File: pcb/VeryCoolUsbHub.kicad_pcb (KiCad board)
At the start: 2 copper layers, 49 parts, among them U1 HD3SS3220RNHR, U2 HD3SS3220RNHR, X1 X322525MSB4SI, X2 X322525MSB4SI

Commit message: BIG UPDATEEEEEEEEE
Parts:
- added C25: CC0603JRNPO9BN390, EasyEDA:C0603, F.Cu at (207.7, 54.3)
- added R2: RC0402FR-0710KL, EasyEDA:R0402, F.Cu at (214.1, 39.1)
- C1, C2, C28, C29, C3, C30, C31, C32, C4, R6: moved to B.Cu
- moved RJ45 155.5 mm to (233.3, 27.6)
- moved USBC_OUT_1 144.3 mm to (243.3, 53.3), turned to 90 degrees
- moved C7 141.6 mm to (244.3, 42.5), turned to -90 degrees
- moved C3 139.3 mm to (246.2, 51.2)
- moved C4 139.0 mm to (246.2, 56.0)
- moved C2 138.7 mm to (246.2, 52.8)
- moved X1 138.3 mm to (240.7, 42.5)
- moved C1 138.3 mm to (246.2, 54.4)
- moved C6 136.5 mm to (240.5, 45.4), turned to 180 degrees
- moved R9 132.3 mm to (225.4, 51.3)
- moved C12 131.7 mm to (239.7, 37.7), turned to 180 degrees
- moved R6 130.6 mm to (233.3, 22.4), turned to 180 degrees
- moved C16 127.4 mm to (235.3, 48.8), turned to 180 degrees
- moved C15 127.1 mm to (235.3, 47.1), turned to 180 degrees
- moved USB_OUT2 125.5 mm to (227.5, 68.8), turned to 180 degrees
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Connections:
- USBC_IN_1 pad 0: unconnected-(USBC_IN_1-EH-Pad0) -> GND
- USB_CONTROLLER1 pad 24: unconnected-(USB_CONTROLLER1-RESETJ-Pad24) -> Net-(USB_CONTROLLER1-RESETJ)
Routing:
- net VBUS: track 13.4 -> 306.7 mm, vias 3 -> 12
- net /V3.3: track 2.57 -> 78.8 mm, vias 2 -> 8
- net /DN0: track 9.16 -> 52.4 mm, vias 2 -> 3
- net /DP0: track 8.09 -> 46.8 mm, vias 2 -> 3
- net /DN3: track 0.00 -> 31.5 mm, vias 0 -> 3
- net /DP3: track 0.00 -> 30.5 mm, vias 0 -> 3
- net /Txp2: track 0.00 -> 29.3 mm, vias 0 -> 1
- net /Txn2: track 0.00 -> 28.7 mm, vias 0 -> 1
- net /LED1: track 0.00 -> 27.1 mm, vias 0 -> 1
- net /LED2: track 0.00 -> 26.9 mm, vias 0 -> 1
- net /RXp2: track 0.00 -> 26.1 mm
- net /DN2: track 0.00 -> 25.9 mm
- net /Txn1: track 0.00 -> 25.6 mm, vias 0 -> 1
- net /RXn2: track 0.00 -> 25.4 mm
- net /Txp1: track 0.00 -> 24.8 mm, vias 0 -> 1
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- added copper zone on B.Cu, net GND
- added copper zone on F.Cu, net GND
- added copper zone on In1.Cu, net GND
- added copper zone on In2.Cu, net GND
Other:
- board outline added: 73.7 x 58.2 mm
- copper layers 2 -> 4
- board text added: "usb controller"

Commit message: please tell me this is the last time i need to reroute
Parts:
- added C26: CC0603KRX7R9BB104, EasyEDA:C0603, F.Cu at (114.6, 62.9)
- added C27: CC0603KRX7R9BB104, EasyEDA:C0603, F.Cu at (114.6, 65.6)
- added C33: CC0603KRX7R9BB104, EasyEDA:C0603, F.Cu at (118.7, 57.6)
- added C34: CC0603KRX7R9BB104, EasyEDA:C0603, F.Cu at (118.7, 60.3)
- C1, C2, C28, C29, C3, C30, C31, C32, C4, R6: moved to F.Cu
- moved C1 140.0 mm to (106.6, 44.2)
- moved C2 139.7 mm to (106.6, 46.9)
- moved C4 139.7 mm to (106.6, 52.2)
- moved C3 139.6 mm to (106.6, 49.6)
- moved C7 138.9 mm to (106.6, 60.3), turned to 0 degrees
- moved C6 134.5 mm to (106.6, 57.6), turned to 0 degrees
- moved C12 129.6 mm to (110.6, 49.6), turned to 0 degrees
- moved C11 126.2 mm to (110.6, 46.9), turned to 0 degrees
- moved C16 125.2 mm to (110.6, 60.3), turned to 0 degrees
- moved C15 125.1 mm to (110.6, 57.6), turned to 0 degrees
- moved C24 122.1 mm to (114.6, 57.6), turned to 0 degrees
- moved C23 122.0 mm to (114.6, 54.9), turned to 0 degrees
- moved C14 121.7 mm to (110.6, 54.9), turned to 0 degrees
- moved C13 118.6 mm to (110.6, 52.2), turned to 0 degrees
- moved C19 117.5 mm to (114.6, 44.2), turned to 0 degrees
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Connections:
- net /RXn0 renamed /RXN0
- net /RXn1 renamed /RXN1
- net /RXn2 renamed /RXN2
- net /RXn3 renamed /RXN3
- net /RXn4 renamed /RXN4
- net /RXp0 renamed /RXP0
- net /RXp1 renamed /RXP1
- net /RXp2 renamed /RXP2
- net /RXp3 renamed /RXP3
- net /RXp4 renamed /RXP4
- net /Txn0 renamed /TXN0
- net /Txn3 renamed /TXN3
- net /Txn4 renamed /TXN4
- net /Txp0 renamed /TXP0
- net /Txp3 renamed /TXP3
- net /Txp4 renamed /TXP4
- USB_CONTROLLER1 pad 47: /Txn1 -> /TXN1
- USB_CONTROLLER1 pad 48: /Txp1 -> /TXP1
- USB_CONTROLLER1 pad 56: /Txn2 -> /TXN2
- USB_CONTROLLER1 pad 57: /Txp2 -> /TXP2
- USB_OUT1 pad 8: /Txn1 -> Net-(USB_OUT1-SSTX-)
- USB_OUT1 pad 9: /Txp1 -> Net-(USB_OUT1-SSTX+)
- USB_OUT2 pad 8: /Txn2 -> Net-(USB_OUT2-SSTX-)
- USB_OUT2 pad 9: /Txp2 -> Net-(USB_OUT2-SSTX+)
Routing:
- net VBUS: track 306.7 -> 8.15 mm, vias 12 -> 4
- net /V3.3: track 78.8 -> 3.42 mm, vias 8 -> 2
- net /DN3: track 31.5 -> 0.00 mm, vias 3 -> 0
- net /DP3: track 30.5 -> 0.00 mm, vias 3 -> 0
- net /Txp2: track 29.3 -> 0.00 mm, vias 1 -> 0
- net /Txn2: track 28.7 -> 0.00 mm, vias 1 -> 0
- net /LED1: track 27.1 -> 0.00 mm, vias 1 -> 0
- net /LED2: track 26.9 -> 0.00 mm, vias 1 -> 0
- net /RXP2: track 26.1 -> 0.00 mm
- net /DN2: track 25.9 -> 0.00 mm
- net /Txn1: track 25.6 -> 0.00 mm, vias 1 -> 0
- net /RXN2: track 25.4 -> 0.00 mm
- net /Txp1: track 24.8 -> 0.00 mm, vias 1 -> 0
- net /RXN1: track 24.6 -> 0.00 mm
- net /DP2: track 24.5 -> 0.00 mm
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- removed copper zone on B.Cu, net GND
- removed copper zone on F.Cu, net GND
- removed copper zone on In1.Cu, net GND
- removed copper zone on In2.Cu, net GND
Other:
- board outline removed
- board text removed: "usb controller"

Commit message: oops forgot to save
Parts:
- removed C10, C26, C27: CC0603KRX7R9BB104, EasyEDA:C0603
- removed USB_OUT1, USB_OUT2: HC-USB3.0-L168-WP, EasyEDA:USB-TH_USB3.0-A
- added C35: CC0603KRX7R9BB104, EasyEDA:C0603, F.Cu at (233.2, 64.7)
- added C36: CC0603KRX7R9BB104, EasyEDA:C0603, B.Cu at (224.2, 65.0)
- added C37: CC0603KRX7R9BB104, EasyEDA:C0603, B.Cu at (225.8, 65.0)
- added R4: R, Resistor_SMD:R_0402_1005Metric, F.Cu at (227.7, 33.2)
- added USB_OUT_1: HC-ST-003-01-J, EasyEDA:USB-3.0-A-TH_HC-ST-003-01-Z, F.Cu at (206.3, 69.6)
- added USB_OUT_2: HC-ST-003-01-J, EasyEDA:USB-3.0-A-TH_HC-ST-003-01-Z, F.Cu at (235.1, 69.7)
- C1, C11, C12, C13, C14, C15, C16, C2, C28, C29, C3, C30, C33, C4: moved to B.Cu
- moved C1 153.1 mm to (259.5, 52.4)
- moved C4 153.0 mm to (259.5, 47.8)
- moved C2 153.0 mm to (259.5, 50.9)
- moved C3 152.9 mm to (259.5, 49.4)
- moved C16 131.0 mm to (239.1, 34.6)
- moved C6 130.4 mm to (234.7, 33.5), turned to 180 degrees
- moved C24 129.9 mm to (244.3, 49.8), turned to 180 degrees
- moved C23 129.8 mm to (244.3, 48.3), turned to 180 degrees
- moved C13 129.5 mm to (239.1, 36.2)
- moved C15 129.5 mm to (239.0, 40.9), turned to 180 degrees
- moved C14 129.3 mm to (239.0, 39.3), turned to 180 degrees
- moved C7 128.3 mm to (231.1, 29.3)
- moved C19 127.0 mm to (241.6, 46.5), turned to 180 degrees
- moved C17 113.7 mm to (222.5, 42.5)
- moved C5 111.7 mm to (217.6, 42.5), turned to 180 degrees
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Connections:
- C11 pad 1: VBUS -> Net-(USB_OUT_1-StdA_SSTX-)
- C11 pad 2: GND -> /TXN1
- C33 pad 2: /TXN2 -> /TXP1
- C34 pad 1: Net-(USB_OUT2-SSTX+) -> VBUS
- C34 pad 2: /TXP2 -> GND
- ETHERNET_CONTROLLER1 pad 38: unconnected-(ETHERNET_CONTROLLER1-RSET-Pad38) -> Net-(ETHERNET_CONTROLLER1-RSET)
- USBC_OUT_1 pad 0: unconnected-(USBC_OUT_1-EH-Pad0) -> GND
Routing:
- net /V3.3: track 3.42 -> 220.7 mm, vias 2 -> 8
- net VBUS: track 8.15 -> 217.5 mm, vias 4 -> 13
- net GND: track 6.98 -> 75.5 mm, vias 8 -> 46
- net /RXN2: track 0.00 -> 43.0 mm
- net /RXP2: track 0.00 -> 40.9 mm
- net /USBC_OUT_RXN1: track 0.00 -> 40.4 mm
- net /USBC_OUT_CC1: track 0.00 -> 40.2 mm, vias 0 -> 2
- net /DN1: track 0.00 -> 39.9 mm
- net /DP1: track 0.00 -> 38.7 mm
- net /USBC_OUT_RXP1: track 0.00 -> 38.5 mm
- net /DP2: track 0.00 -> 38.3 mm
- net /LED2: track 0.00 -> 38.1 mm
- net /DP3: track 0.00 -> 37.4 mm, vias 0 -> 3
- net /DN2: track 0.00 -> 37.1 mm
- net /RXP1: track 0.00 -> 36.6 mm
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- added copper zone on B.Cu, net GND
- added copper zone on In1.Cu, net GND
- added copper zone on In2.Cu, net GND
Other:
- board outline added: 84.8 x 58.4 mm

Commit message: LETSGO THIS GONNA BE THE LAST TIME I ROUTE
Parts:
- added C10: CC0603KRX7R9BB104, EasyEDA:C0603, F.Cu at (230.7, 60.8)
- added C26: CC0603KRX7R9BB104, EasyEDA:C0603, F.Cu at (230.7, 62.3)
- C11, C12, C13, C14, C15, C16, C33, C36, C37: moved to F.Cu
- C31, C32, R6: moved to B.Cu
- moved C16 25.5 mm to (220.5, 52.1)
- moved C13 23.5 mm to (220.5, 50.5)
- moved C31 22.7 mm to (167.4, 57.3), turned to 0 degrees
- moved C32 22.7 mm to (167.4, 55.8), turned to 180 degrees
- moved R4 22.3 mm to (209.2, 45.6), turned to 180 degrees
- moved RJ45 21.3 mm to (200.1, 38.4)
- moved ETHERNET_CONTROLLER1 21.2 mm to (212.7, 48.9)
- moved C6 20.8 mm to (216.2, 43.1), turned to -90 degrees
- moved C14 20.7 mm to (219.6, 46.4)
- moved C15 20.7 mm to (219.6, 48.0)
- moved X1 20.7 mm to (213.3, 43.0)
- moved C7 20.7 mm to (213.2, 39.6)
- moved C35 20.2 mm to (216.2, 75.7), turned to 90 degrees
- moved C4 19.6 mm to (242.2, 57.1)
- moved C19 19.5 mm to (223.1, 52.7), turned to -90 degrees
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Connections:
- C11 pad 2: /TXN1 -> /TXP1
- C20 pad 1: /USBC_IN_TXP2 -> /USBC_IN_TXN2
- C21 pad 1: /USBC_IN_TXN2 -> /USBC_IN_TXP2
- C23 pad 1: /USBC_OUT_TXP2 -> /USBC_OUT_TXN2
- C24 pad 1: /USBC_OUT_TXN2 -> /USBC_OUT_TXP2
- C33 pad 2: /TXP1 -> /TXN1
- C35 pad 1: Net-(USB_OUT_2-Vbus) -> VBUS
- C36 pad 2: /TXN2 -> /TXP2
- C37 pad 2: /TXP2 -> /TXN2
- C8 pad 1: /USBC_IN_TXN1 -> /USBC_IN_TXP1
- C9 pad 2: /USBC_IN_TXP1 -> /USBC_IN_TXN1
- ETHERNET_CONTROLLER1 pad 12: /TXN4 -> /TXP4
- ETHERNET_CONTROLLER1 pad 13: /TXP4 -> /TXN4
- ETHERNET_CONTROLLER1 pad 15: /RXN4 -> /RXP4
- ETHERNET_CONTROLLER1 pad 16: /RXP4 -> /RXN4
- U1 pad 16: /USBC_OUT_TXN1 -> Net-(U1-TX1n)
- U1 pad 17: /USBC_OUT_TXP1 -> Net-(U1-TX1p)
- USB_OUT_1 pad 5: /RXN1 -> /RXP1
- USB_OUT_1 pad 6: /RXP1 -> /RXN1
- USB_OUT_2 pad 1: Net-(USB_OUT_2-Vbus) -> VBUS
- USB_OUT_2 pad 5: /RXN2 -> /RXP2
- USB_OUT_2 pad 6: /RXP2 -> /RXN2
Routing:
- net /V3.3: track 220.7 -> 104.0 mm, vias 8 -> 7
- net VBUS: track 217.5 -> 285.5 mm, vias 13 -> 12
- net GND: track 75.5 -> 101.7 mm, vias 46 -> 37
- net /RXP1: track 36.6 -> 16.9 mm
- net /RXN1: track 35.6 -> 16.9 mm
- net /USBC_IN_CC2: track 25.5 -> 42.0 mm
- net /DN2: track 37.1 -> 53.3 mm
- net /USBC_OUT_TXN2: track 12.3 -> 27.6 mm, vias 2 -> 0
- net /USBC_OUT_TXP2: track 12.5 -> 26.3 mm, vias 2 -> 0
- net /DP2: track 38.3 -> 52.1 mm
- net /USBC_IN_RXP1: track 22.2 -> 35.8 mm
- net /RXN2: track 43.0 -> 29.3 mm
- net /USBC_IN_TXN2: track 16.1 -> 29.7 mm, vias 2 -> 0
- net /USBC_IN_RXN1: track 24.1 -> 37.7 mm
- net Net-(USB_OUT_2-StdA_SSTX-): track 21.9 -> 8.87 mm
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- removed copper zone on B.Cu, net GND
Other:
- board size 84.8 x 58.4 mm -> 80.7 x 55.9 mm

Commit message: maybedone?
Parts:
- added G***: LOGO, LOGO, F.Cu at (229.0, 49.2)
- added G***: LOGO, LOGO, F.Cu at (240.0, 74.4)
- added G***: LOGO, LOGO, F.Cu at (179.6, 35.8)
- added G***: LOGO, LOGO, F.Cu at (172.7, 31.7)
- added G***: LOGO, LOGO, F.Cu at (233.1, 35.2)
- added G***: LOGO, LOGO, F.Cu at (187.6, 72.7)
- added G***: LOGO, LOGO, F.Cu at (174.4, 46.0)
- moved R2 1.36 mm to (204.5, 52.4)
- moved C5 1.34 mm to (201.2, 52.4)
- moved C17 1.14 mm to (207.5, 52.1)
- renumbered USBC_IN_1 to USB_IN_1
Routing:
- net VBUS: track 285.5 -> 331.4 mm, vias 12 -> 11
- net GND: track 101.7 -> 116.4 mm, vias 37 -> 40
- net /USBC_IN_RXP1: track 35.8 -> 28.0 mm
- net /USBC_IN_RXN1: track 37.7 -> 29.9 mm
- net /USBC_IN_TXN2: track 29.7 -> 22.2 mm
- net /USBC_IN_TXP2: track 28.5 -> 20.9 mm
- net /USBC_IN_CC2: track 42.0 -> 40.4 mm
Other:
- outline, holes or cut-outs redrawn
- board text added: "1 Gb Ethernetport"
- board text added: "@duykhanh09103"
- board text added: "Ethernet Controler"
- board text added: "Opensource project!!"
- board text added: "Specical shoutout: TobyCM Arca Keyaan Astra Celestine Cyao"
- board text added: "USB A DOWNSTREAM"
- board text added: "USB C DOWNSTREAM"
- board text added: "USB C UPSTREAM"
- board text added: "USB Controller"
- board text added: "made with love from duykhanh09103 <3 me@duykhanh09103.dev"

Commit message: i think im done with pcb
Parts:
- added G***: LOGO, LOGO, B.Cu at (212.1, 57.0)
- added G***: LOGO, LOGO, B.Cu at (171.0, 37.7)
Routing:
- net GND: track 116.4 -> 114.8 mm, vias 40 -> 39
- net VBUS: track 331.4 -> 330.3 mm
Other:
- board text added: "This project is sponsored by fallout!!"
- board text added: "pss, join hackclub here"

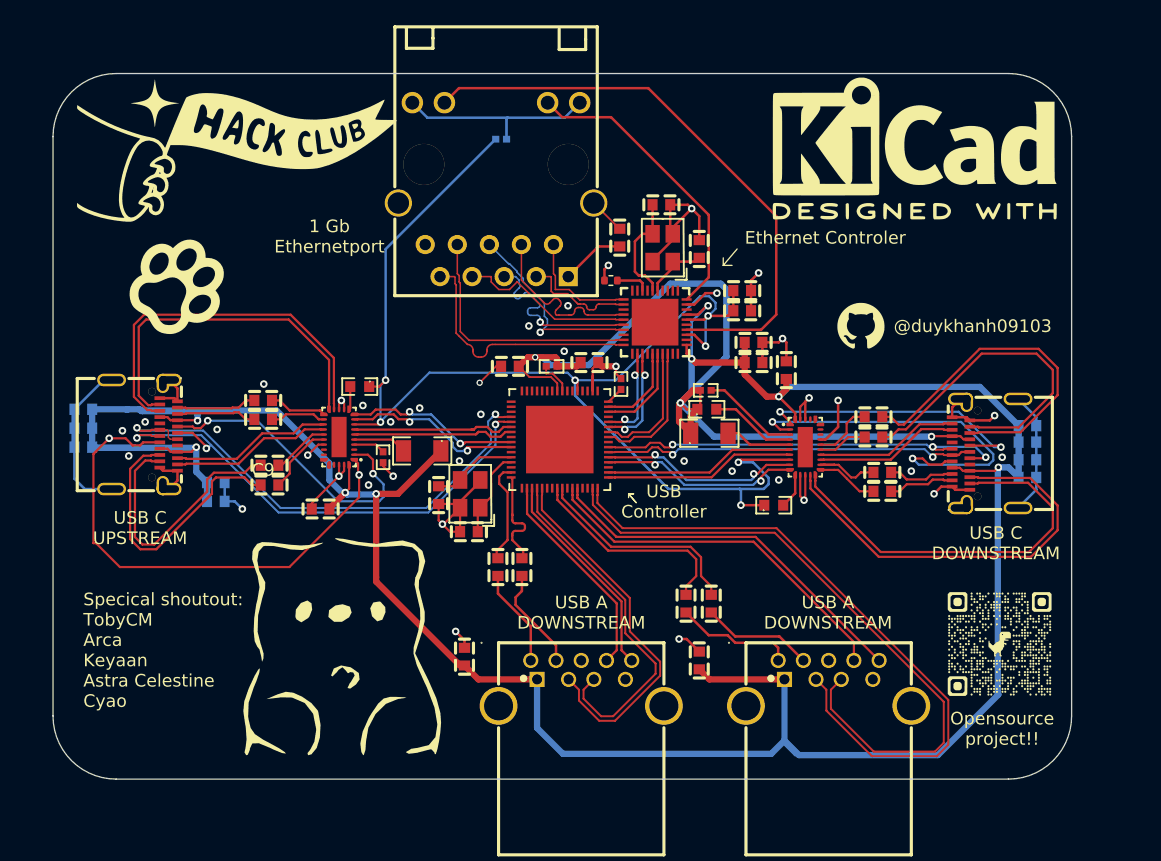
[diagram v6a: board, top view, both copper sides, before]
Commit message: add VBUS plane to last layer
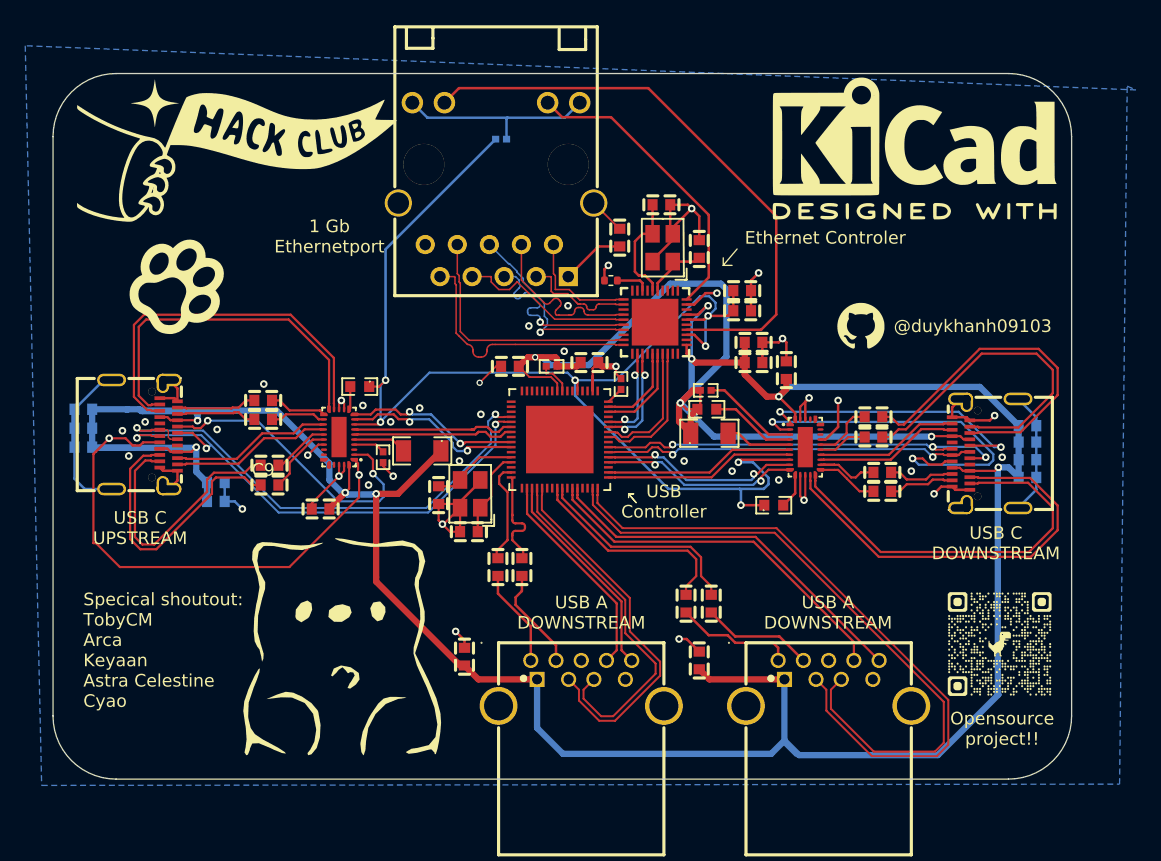
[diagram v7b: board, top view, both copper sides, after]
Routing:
- added copper zone on B.Cu, net VBUS
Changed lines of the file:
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@@
+	)
+	(zone
+		(net 2)
+		(net_name "VBUS")
+		(layer "B.Cu")
+		(hatch edge 0.5)
+		(priority 1)
+		(connect_pads
+			(clearance 0.5)
+		)
+		(min_thickness 0.25)
+		(filled_areas_thickness no)
+		(fill yes
+			(thermal_gap 0.5)
+			(thermal_bridge_width 0.5)
+		)
+		(polygon
+			(pts
+				(xy 250.8 30.5) (xy 162.8 27) (xy 164.1 85.6) (xy 249.5 85.5) (xy 250.1 30.2)
+			)
+		)
 	)
 	(zone
@@
 		(hatch edge 0.5)
 		(connect_pads
-			(clearance 0.5)
+			(clearance 0.3)
 		)
 		(min_thickness 0.25)

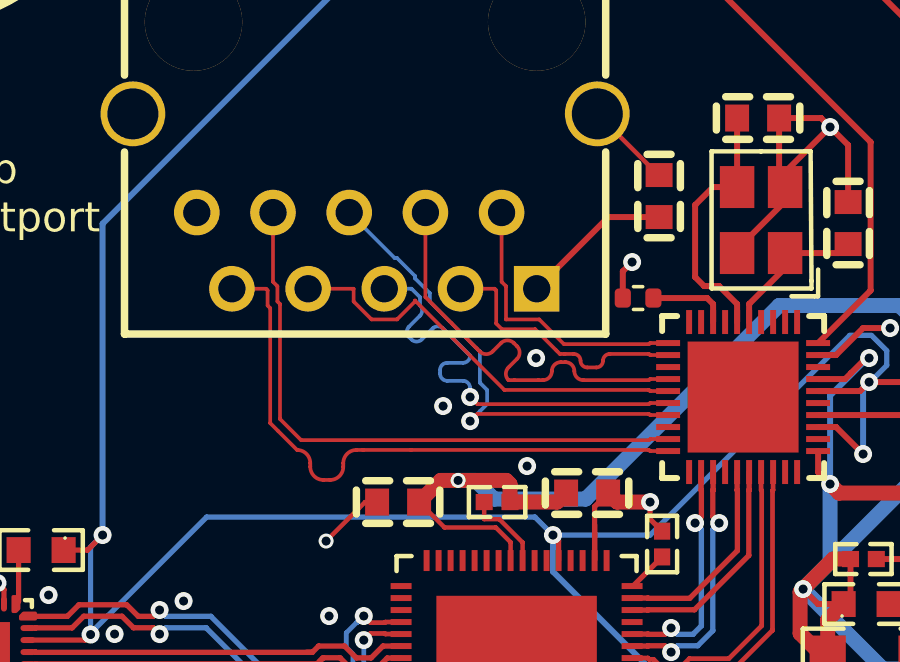
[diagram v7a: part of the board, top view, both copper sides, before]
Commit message: reroute a litlle bit of ethernet port
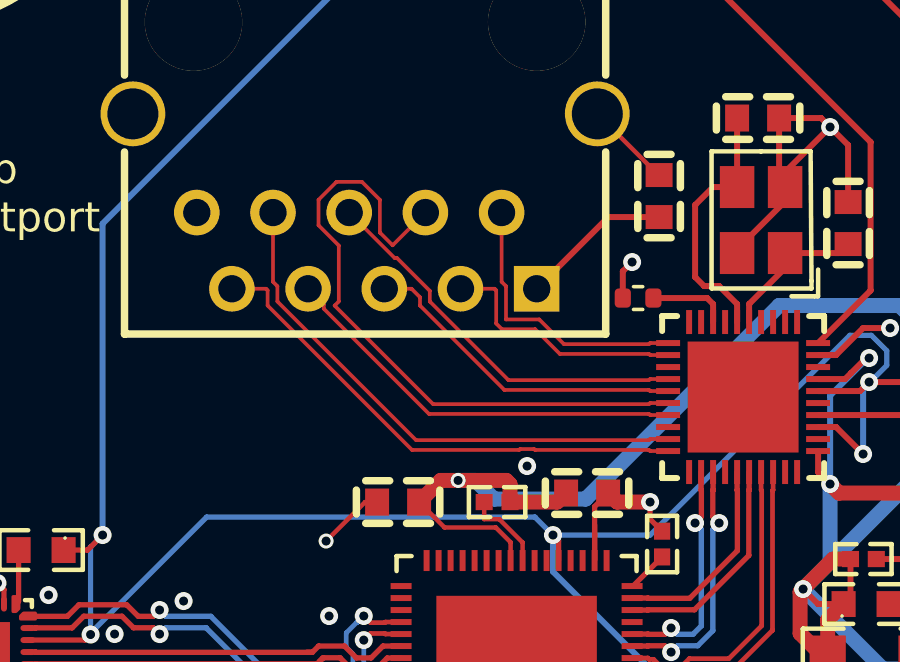
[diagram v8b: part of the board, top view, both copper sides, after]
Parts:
- renumbered USB_IN_1 to USBC_IN_1
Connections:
- ETHERNET_CONTROLLER1 pad 4: /MDIP1 -> /MDIN2
- ETHERNET_CONTROLLER1 pad 5: /MDIN1 -> /MDIP2
- ETHERNET_CONTROLLER1 pad 6: /MDIP2 -> /MDIP1
- ETHERNET_CONTROLLER1 pad 7: /MDIN2 -> /MDIN1
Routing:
- net /MDIP1: track 14.1 -> 22.1 mm
- net /MDIP2: track 15.1 -> 11.0 mm, vias 1 -> 0
- net /MDIN3: track 20.5 -> 17.1 mm
- net /MDIN2: track 15.8 -> 13.2 mm, vias 1 -> 0
- net /MDIP3: track 20.2 -> 18.0 mm
- net GND: vias 39 -> 37
